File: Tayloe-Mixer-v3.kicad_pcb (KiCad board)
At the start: 2 copper layers, 112 x 78.5 mm, 61 parts, among them J1 BNC, J101 Audio_Jack, J2 Conn_01x04, J3 Pad, J4 Conn_01x07_Female, J5 Pad, Q1 2N3904-SMD, Q2 2N3904-SMD, SW1 SW_DIP_x01, SW2 Rotary_Encoder_Switch, T1 6:31, T2 31:6, T3 T50_SPLITTER, U1 ESP32-A1S, U2 FST3253, U201 MAR6, U3 LM4562, U4 si5351, U5 L7805, U7 AMS1117CD-3.3

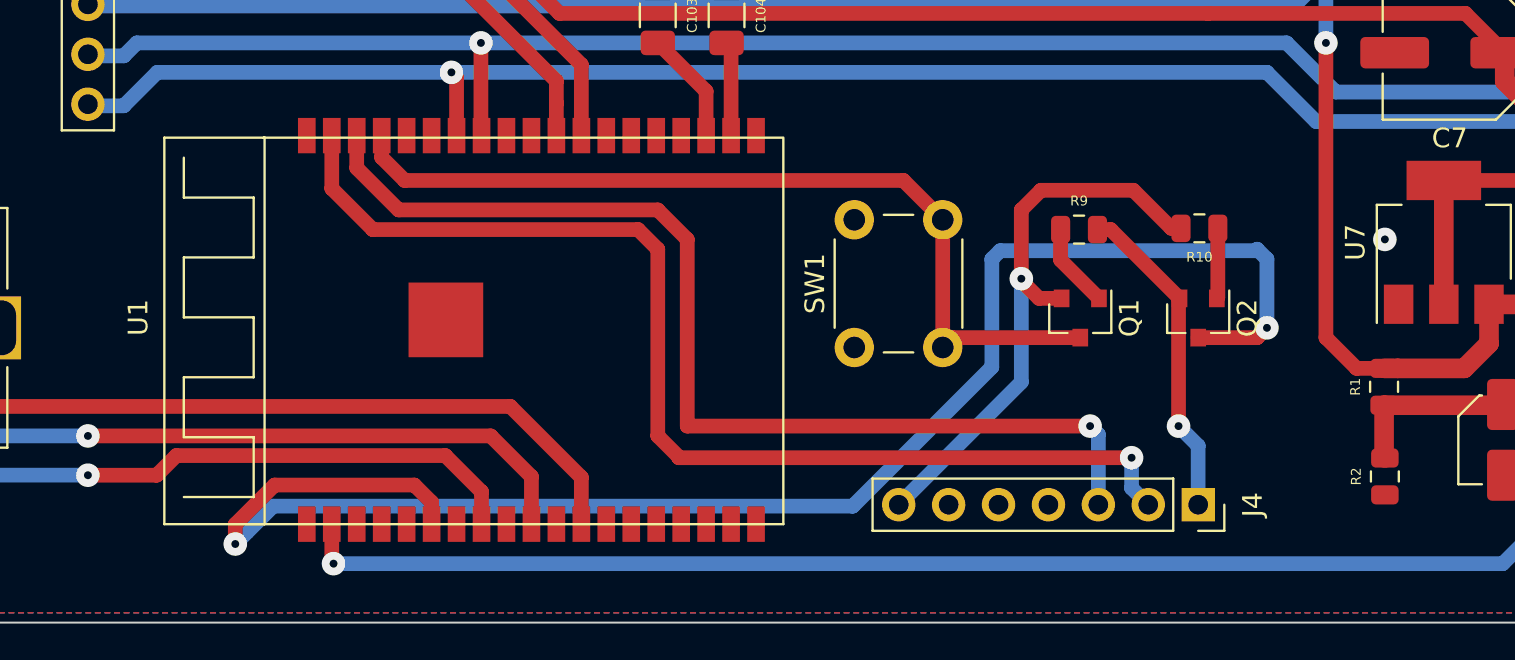
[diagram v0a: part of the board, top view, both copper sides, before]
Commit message: fixed rx/tx
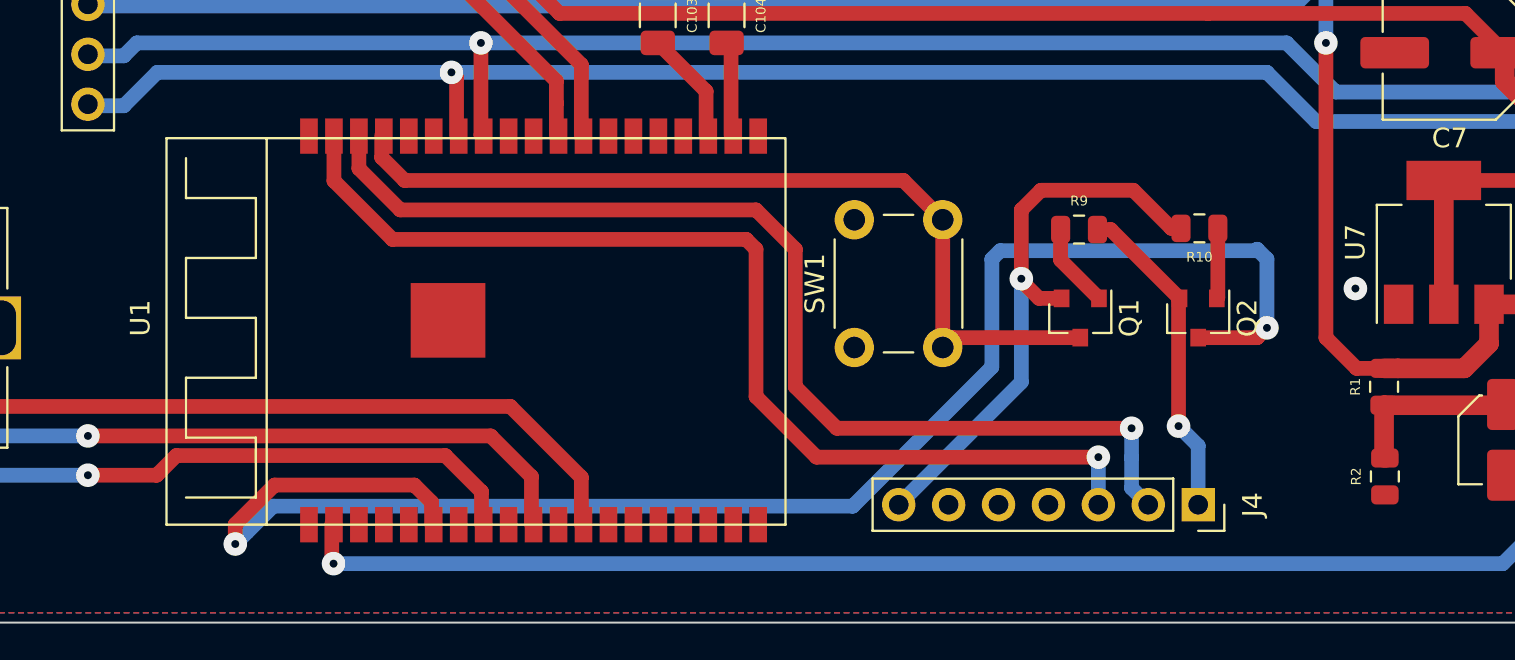
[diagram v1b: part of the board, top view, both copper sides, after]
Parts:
- U1: footprint xenir:ESP32-A1S -> Xenir:ESP32-A1S
- moved U1 0.11 mm to (69.0, 88.5)
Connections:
- J4 pad 2: TX0 -> RX0
- J4 pad 3: RX0 -> TX0
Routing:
- net TX0: track 57.4 -> 53.8 mm
- net RX0: track 54.1 -> 54.8 mm

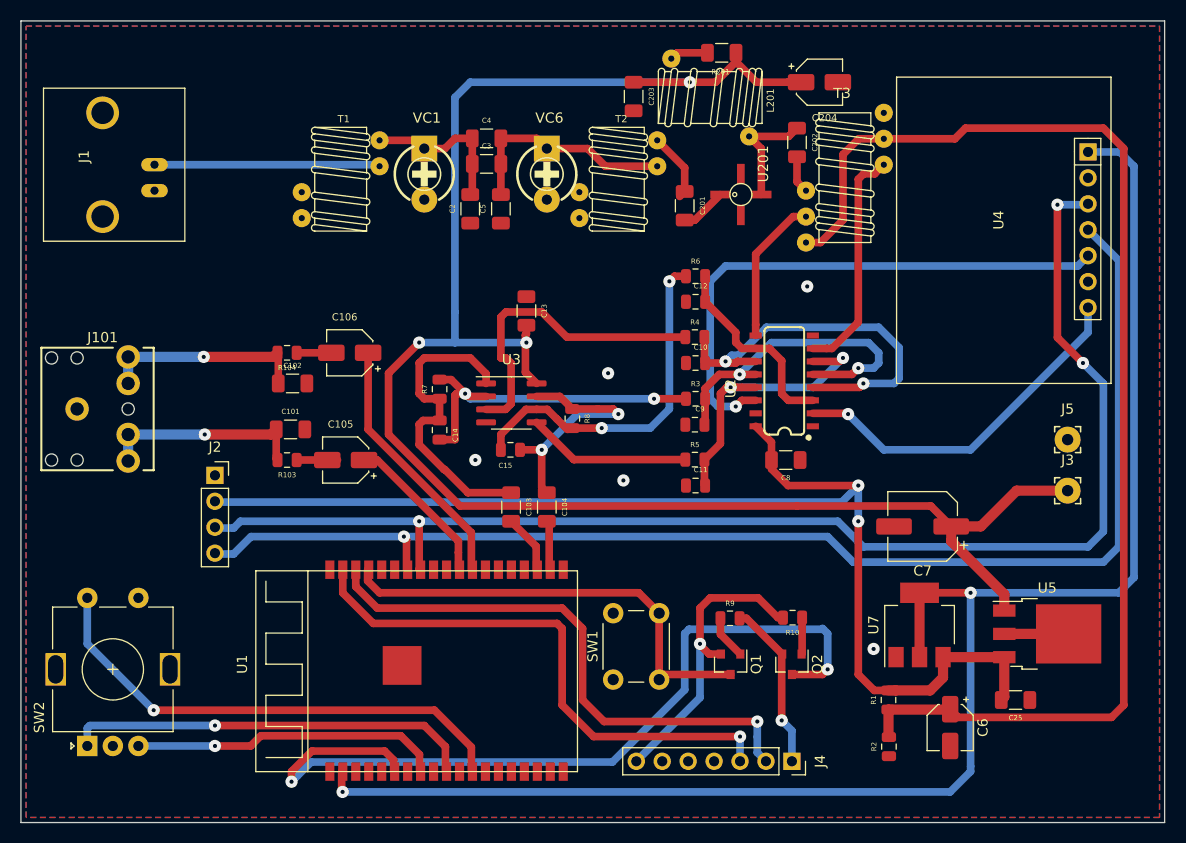
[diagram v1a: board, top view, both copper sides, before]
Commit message: added keepout area under esp32
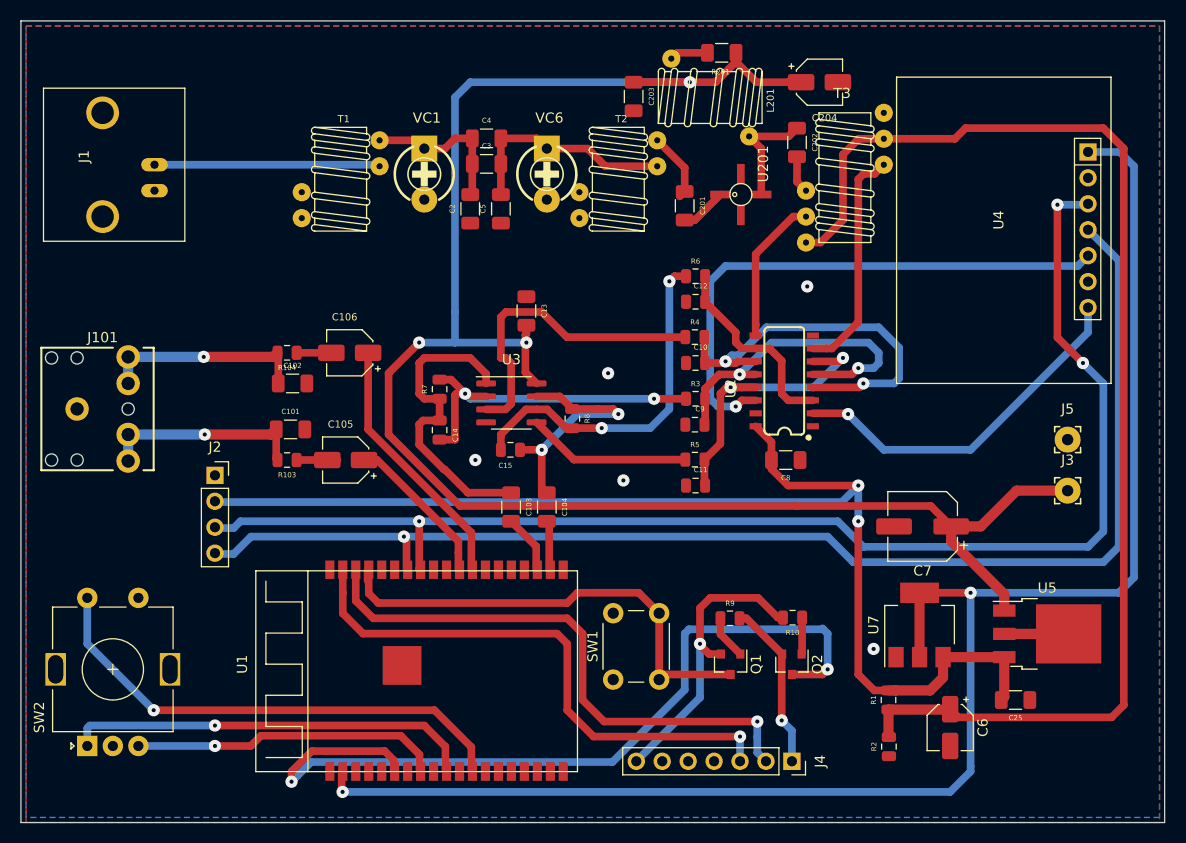
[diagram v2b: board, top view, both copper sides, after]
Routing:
- net EN: track 44.7 -> 47.2 mm
- net TX0: track 53.8 -> 54.4 mm
- net RX0: track 54.8 -> 55.3 mm
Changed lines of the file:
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@@
     (thickness 1.6)
     (drawings 4)
-    (tracks 452)
+    (tracks 456)
     (zones 0)
     (modules 61)
@@
   (segment (start 114 89) (end 107.5 89) (width 0.75) (layer F.Cu) (net 19))
   (segment (start 107 83) (end 107 89.5) (width 0.75) (layer F.Cu) (net 19))
-  (segment (start 78.45 79.832002) (end 79.617998 81) (width 0.75) (layer F.Cu) (net 19))
   (segment (start 78.45 78.717) (end 78.45 79.832002) (width 0.75) (layer F.Cu) (net 19))
   (segment (start 105 81) (end 107 83) (width 0.75) (layer F.Cu) (net 19))
-  (segment (start 79.617998 81) (end 105 81) (width 0.75) (layer F.Cu) (net 19))
+  (segment (start 105 81) (end 99 81) (width 0.75) (layer F.Cu) (net 19))
+  (segment (start 99 81) (end 98 82) (width 0.75) (layer F.Cu) (net 19))
+  (segment (start 98 82) (end 79.5 82) (width 0.75) (layer F.Cu) (net 19))
+  (segment (start 78.56 81.06) (end 78.56 78.742) (width 0.75) (layer F.Cu) (net 19))
+  (segment (start 79.5 82) (end 78.56 81.06) (width 0.75) (layer F.Cu) (net 19))
   (segment (start 118.6375 83.4375) (end 116.7 81.5) (width 0.75) (layer F.Cu) (net 20))
   (segment (start 119.125 83.4375) (end 118.6375 83.4375) (width 0.75) (layer F.Cu) (net 20))
@@
   (segment (start 85 92.5) (end 88.61 96.11) (width 0.75) (layer F.Cu) (net 26))
   (segment (start 57.5 92.5) (end 85 92.5) (width 0.75) (layer F.Cu) (net 26))
+  (segment (start 114.92 97.5) (end 114.92 95.08) (width 0.75) (layer B.Cu) (net 39))
+  (segment (start 114.92 95.08) (end 114.92 95.08) (width 0.75) (layer B.Cu) (net 39))
+  (via (at 114.92 95.08) (size 1.2) (drill 0.4) (layers F.Cu B.Cu) (net 39))
+  (segment (start 76.02 81.02) (end 76.02 78.742) (width 0.75) (layer F.Cu) (net 39))
+  (segment (start 76.02 83.02) (end 76.02 81.02) (width 0.75) (layer F.Cu) (net 39))
+  (segment (start 78 85) (end 76.02 83.02) (width 0.75) (layer F.Cu) (net 39))
+  (segment (start 97 85) (end 78 85) (width 0.75) (layer F.Cu) (net 39))
+  (segment (start 98 86) (end 97 85) (width 0.75) (layer F.Cu) (net 39))
+  (segment (start 98 92.5) (end 98 86) (width 0.75) (layer F.Cu) (net 39))
+  (segment (start 100.58 95.08) (end 98 92.5) (width 0.75) (layer F.Cu) (net 39))
+  (segment (start 114.92 95.08) (end 100.58 95.08) (width 0.75) (layer F.Cu) (net 39))
   (segment (start 117.46 97.5) (end 116.610001 96.650001) (width 0.75) (layer B.Cu) (net 40))
   (segment (start 116.610001 96.650001) (end 116.610001 95.110001) (width 0.75) (layer B.Cu) (net 40))
@@
   (segment (start 116.610001 93.610001) (end 116.610001 93.610001) (width 0.75) (layer B.Cu) (net 40))
   (via (at 116.610001 93.610001) (size 1.2) (drill 0.4) (layers F.Cu B.Cu) (net 40))
-  (segment (start 114.92 97.5) (end 114.92 95.08) (width 0.75) (layer B.Cu) (net 39))
-  (segment (start 114.92 95.08) (end 114.92 95.08) (width 0.75) (layer B.Cu) (net 39))
-  (via (at 114.92 95.08) (size 1.2) (drill 0.4) (layers F.Cu B.Cu) (net 39))
-  (segment (start 100.58 95.08) (end 114.92 95.08) (width 0.75) (layer F.Cu) (net 39))
-  (segment (start 97.5 92) (end 100.58 95.08) (width 0.75) (layer F.Cu) (net 39))
-  (segment (start 97.5 84.5) (end 97.5 92) (width 0.75) (layer F.Cu) (net 39))
-  (segment (start 97 84) (end 97.5 84.5) (width 0.75) (layer F.Cu) (net 39))
-  (segment (start 79 84) (end 97 84) (width 0.75) (layer F.Cu) (net 39))
-  (segment (start 76.02 81.02) (end 79 84) (width 0.75) (layer F.Cu) (net 39))
-  (segment (start 76.02 78.742) (end 76.02 81.02) (width 0.75) (layer F.Cu) (net 39))
-  (segment (start 77.29 80.392) (end 79.398 82.5) (width 0.75) (layer F.Cu) (net 40))
-  (segment (start 77.29 78.742) (end 77.29 80.392) (width 0.75) (layer F.Cu) (net 40))
-  (segment (start 79.398 82.5) (end 97.5 82.5) (width 0.75) (layer F.Cu) (net 40))
-  (segment (start 97.5 82.5) (end 99.5 84.5) (width 0.75) (layer F.Cu) (net 40))
-  (segment (start 99.5 84.5) (end 99.5 91.5) (width 0.75) (layer F.Cu) (net 40))
   (segment (start 101.610001 93.610001) (end 116.610001 93.610001) (width 0.75) (layer F.Cu) (net 40))
   (segment (start 99.5 91.5) (end 101.610001 93.610001) (width 0.75) (layer F.Cu) (net 40))
+  (segment (start 99.5 85) (end 99.5 91.5) (width 0.75) (layer F.Cu) (net 40))
+  (segment (start 98 83.5) (end 99.5 85) (width 0.75) (layer F.Cu) (net 40))
+  (segment (start 79 83.5) (end 98 83.5) (width 0.75) (layer F.Cu) (net 40))
+  (segment (start 77.29 81.79) (end 79 83.5) (width 0.75) (layer F.Cu) (net 40))
+  (segment (start 77.29 78.742) (end 77.29 81.79) (width 0.75) (layer F.Cu) (net 40))
   (segment (start 110.5 44.5) (end 113 42) (width 0.75) (layer F.Cu) (net 49))
   (segment (start 109.5 44.5) (end 110.5 44.5) (width 0.75) (layer F.Cu) (net 49))
@@
   (segment (start 152.5 92) (end 152.5 37.5) (width 0.75) (layer F.Cu) (net 71))
   (segment (start 135.5 92.4) (end 136.3 93.2) (width 0.75) (layer F.Cu) (net 71))
+  (zone (net 0) (net_name "") (layer F.Cu) (hatch edge 0.508)
+    (connect_pads (clearance 0.508))
+    (min_thickness 0.254)
+    (keepout (tracks not_allowed) (vias not_allowed) (copperpour not_allowed))
+    (fill (arc_segments 32) (thermal_gap 0.508) (thermal_bridge_width 0.508))
+    (polygon
+      (pts
+        (xy 97 97) (xy 89.5 97) (xy 89.5 93) (xy 97 93)
+      )
+    )
+  )
+  (zone (net 0) (net_name "") (layer F.Cu) (hatch edge 0.508)
+    (connect_pads (clearance 0.508))
+    (min_thickness 0.254)
+    (keepout (tracks not_allowed) (vias not_allowed) (copperpour not_allowed))
+    (fill (arc_segments 32) (thermal_gap 0.508) (thermal_bridge_width 0.508))
+    (polygon
+      (pts
+        (xy 97.5 81.5) (xy 80 81.5) (xy 80 80) (xy 97.5 80)
+      )
+    )
+  )
   (zone (net 1) (net_name GND) (layer F.Cu) (hatch edge 0.508)
     (connect_pads (clearance 0.508))
@@
     (polygon
       (pts
-        (xy 156 103) (xy 45 103) (xy 45 25.5) (xy 156 25.5)
+        (xy 156 103.5) (xy 45 103.5) (xy 45 25.5) (xy 156 25.5)
       )
     )
